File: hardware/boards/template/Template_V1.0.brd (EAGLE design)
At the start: 42 x 42 mm, 2 parts

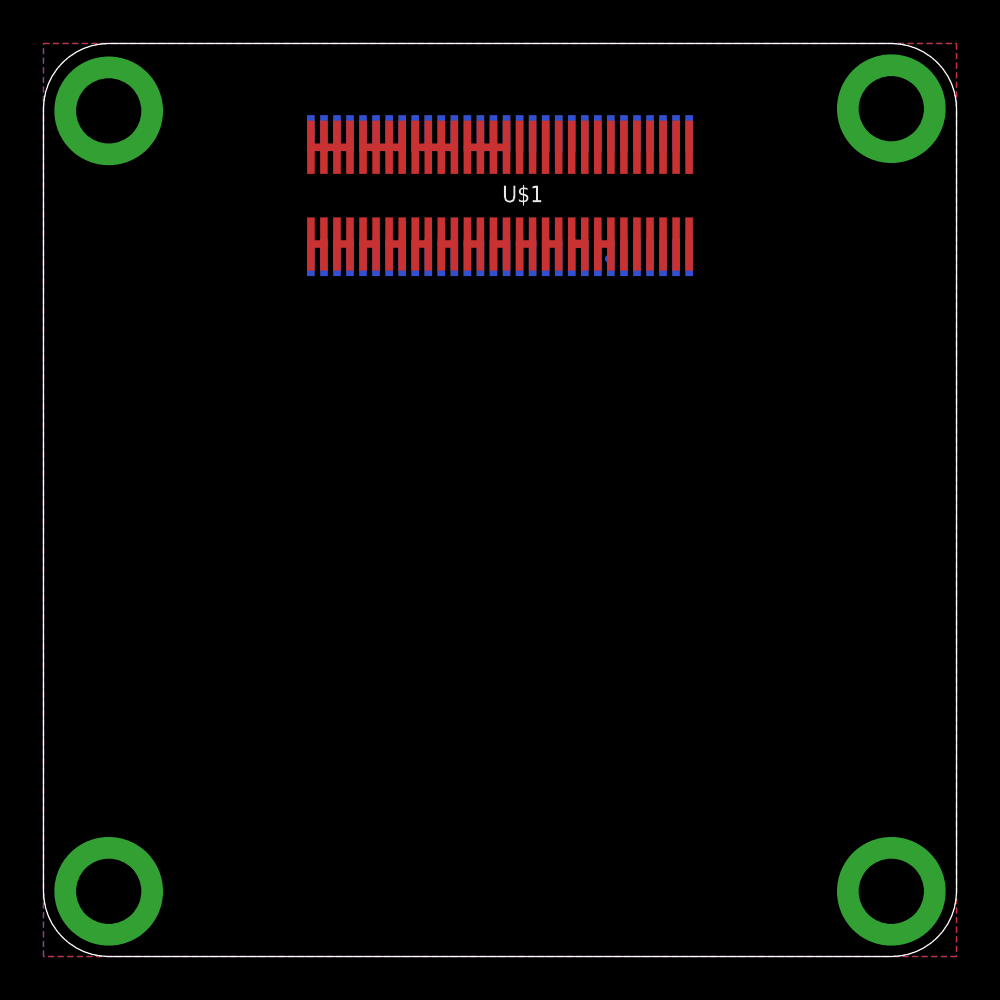
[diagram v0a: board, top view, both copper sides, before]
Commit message: Finished updating to new PQ60 V1.1 standard
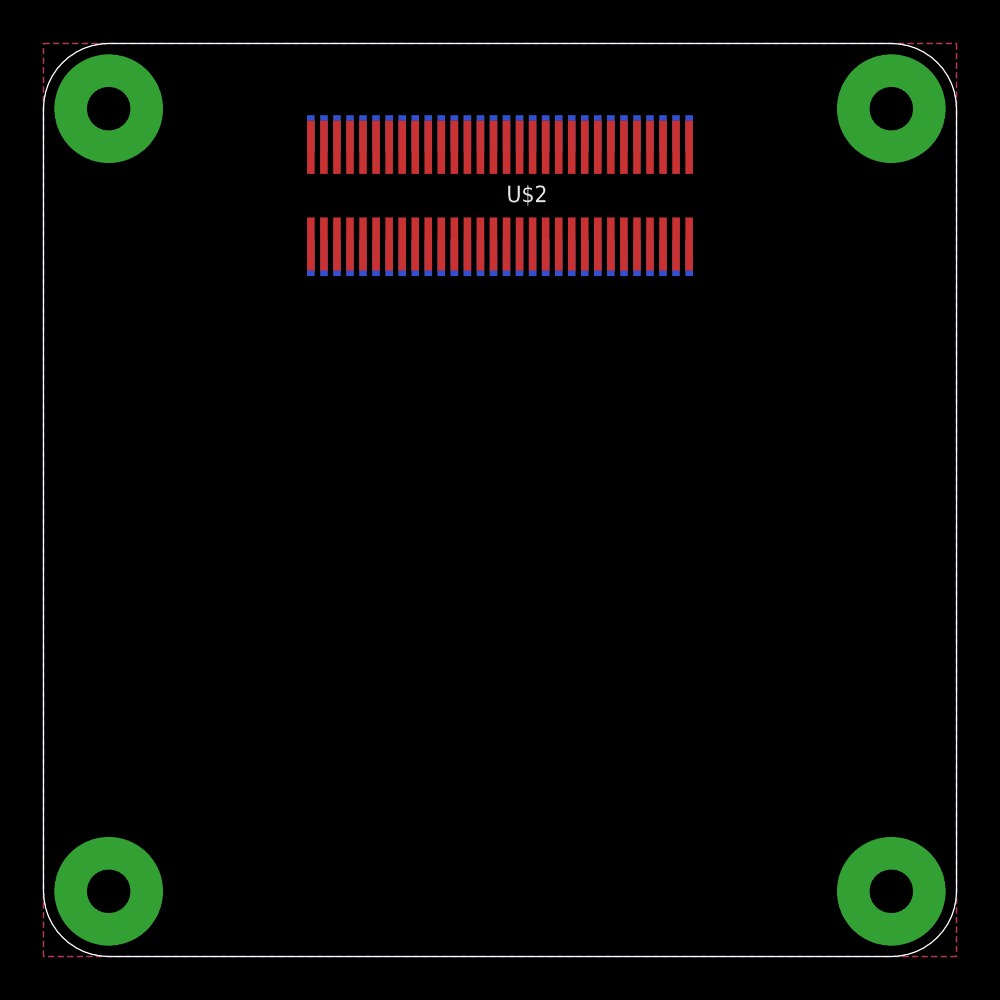
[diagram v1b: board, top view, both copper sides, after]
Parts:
- removed U$3: FX8C-060S-SV(92), PQ_components:FX8C-060S-SV(92)
- added U$2: FX8C-060P-SV(92), Template:FX8C-060P-SV(92)
- U$1: value FX8C-060P-SV(92) -> FX8C-060S-SV(92); device PQ_components:FX8C-060P-SV(92) -> Template:FX8C-060S-SV(92)
- flipped U$1 to the bottom, turned to 180 degrees
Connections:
- removed net +3.3V_1: U$3.P$22
- removed net +3.3V_2: U$3.P$21
- removed net +3.3V_3: U$3.P$20
- removed net 33-GND: U$3.P$3
- removed net 37-GND: U$3.P$7
- removed net 41-GND: U$3.P$11
- removed net 44-GND: U$3.P$14
- removed net 46-GND: U$3.P$16
- removed net 48-GND: U$3.P$18
- removed net 49-GND: U$3.P$19
- removed net 57-GND: U$3.P$27
- removed net 59-GND: U$3.P$29
- removed net VBUS2: U$3.P$24
- net +3.3V_SW1: now also U$2.P$1, U$2.P$2; no longer U$3.P$59, U$3.P$60
- net +3V3_BUS: now also U$2.P$57, U$2.P$58, U$2.P$59, U$2.P$60
- net +3V3_SW2: now also U$2.P$5, U$2.P$6; no longer U$3.P$55, U$3.P$56
- net +3V3_SW3: now also U$2.P$10, U$2.P$9; no longer U$3.P$51, U$3.P$52
- net /RST: now also U$2.P$27; no longer U$3.P$34
- net /SS/GPIO2: now also U$2.P$34
- net BATV_BUS: now also U$2.P$49, U$2.P$50, U$2.P$51, U$2.P$52
- net BATV_SW1: now also U$2.P$13, U$2.P$14; no longer U$3.P$47, U$3.P$48
- net BATV_SW2: now also U$2.P$17, U$2.P$18; no longer U$3.P$43, U$3.P$44
- net BATV_SW3: now also U$2.P$21, U$2.P$22; no longer U$3.P$39, U$3.P$40
- net GND: now also U$2.P$28; no longer U$3.P$33
- net GPIO0: now also U$2.P$25; no longer U$3.P$36
- net GPIO1: now also U$2.P$26; no longer U$3.P$35
- net GPIO10: now also U$2.P$42
- net GPIO11: now also U$2.P$43
- net GPIO12: now also U$2.P$44
- net GPIO3: now also U$2.P$35
- net GPIO4: now also U$2.P$36
- net GPIO5: now also U$2.P$37
- net GPIO6: now also U$2.P$38
- net GPIO7: now also U$2.P$39
- net GPIO8: now also U$2.P$40
- net GPIO9: now also U$2.P$41
- net MISO: now also U$2.P$32
- net MOSI: now also U$2.P$31
- net RTN_+3V3: now also U$2.P$53, U$2.P$54, U$2.P$55, U$2.P$56
- net RTN_+3V3_SW1: now also U$2.P$3, U$2.P$4; no longer U$3.P$57, U$3.P$58
- net RTN_+3V3_SW2: now also U$2.P$7, U$2.P$8; no longer U$3.P$53, U$3.P$54
- net RTN_+3V3_SW3: now also U$2.P$11, U$2.P$12; no longer U$3.P$49, U$3.P$50
- net RTN_BATV: now also U$2.P$45, U$2.P$46, U$2.P$47, U$2.P$48
- net RTN_BATV_SW1: now also U$2.P$15, U$2.P$16; no longer U$3.P$45, U$3.P$46
- net RTN_BATV_SW2: now also U$2.P$19, U$2.P$20; no longer U$3.P$41, U$3.P$42
- net RTN_BATV_SW3: now also U$2.P$23, U$2.P$24; no longer U$3.P$37, U$3.P$38
- net SCK: now also U$2.P$33
- net SCL: now also U$2.P$29; no longer U$3.P$32
- net SDA: now also U$2.P$30; no longer U$3.P$31
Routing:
- net RTN_BATV: track 1.80 -> 0.00 mm
- net RTN_+3V3: track 1.80 -> 0.00 mm
- net +3V3_BUS: track 1.80 -> 0.00 mm
- net BATV_BUS: track 1.80 -> 0.00 mm
- net BATV_SW3: track 1.11 -> 0.00 mm
- net RTN_BATV_SW3: track 0.72 -> 0.00 mm
- net RTN_BATV_SW1: track 0.60 -> 0.00 mm
- net BATV_SW2: track 0.60 -> 0.00 mm
- net BATV_SW1: track 0.60 -> 0.00 mm
- net +3V3_SW2: track 0.60 -> 0.00 mm
- net RTN_+3V3_SW2: track 0.60 -> 0.00 mm
- net RTN_+3V3_SW1: track 0.60 -> 0.00 mm
- net +3.3V_SW1: track 0.60 -> 0.00 mm
- net RTN_BATV_SW2: track 0.60 -> 0.00 mm
- net RTN_+3V3_SW3: track 0.60 -> 0.00 mm
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- added copper zone on layer 1, net BOARD
- added copper zone on layer 16, net BOARD
- removed copper zone on layer 1, net GND
- removed copper zone on layer 16, net N$1
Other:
- board text added: "SurreyEARS Pocketqube"
- board text added: "Template Board"
- board text added: "V1.0"

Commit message: fixed fx8c symbols
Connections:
- new net +3V3_SW1: U$1.P$1
- net +3.3V_SW1: no longer U$1.P$1
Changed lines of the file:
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@@
 </signal>
 <signal name="RTN_+3V3">
+<contactref element="U$2" pad="P$53"/>
+<contactref element="U$2" pad="P$54"/>
+<contactref element="U$2" pad="P$55"/>
 <contactref element="U$2" pad="P$56"/>
-<contactref element="U$2" pad="P$55"/>
-<contactref element="U$2" pad="P$54"/>
-<contactref element="U$2" pad="P$53"/>
+<contactref element="U$1" pad="P$53"/>
+<contactref element="U$1" pad="P$54"/>
+<contactref element="U$1" pad="P$55"/>
 <contactref element="U$1" pad="P$56"/>
-<contactref element="U$1" pad="P$55"/>
-<contactref element="U$1" pad="P$54"/>
-<contactref element="U$1" pad="P$53"/>
-<wire x1="15.9" y1="37.225" x2="15.3" y2="37.225" width="0" layer="19" extent="1-1"/>
-<wire x1="16.5" y1="37.225" x2="15.9" y2="37.225" width="0" layer="19" extent="1-1"/>
+<wire x1="15.3" y1="37.225" x2="15.3" y2="37.225" width="0" layer="19" extent="1-1"/>
+<wire x1="14.7" y1="37.225" x2="15.3" y2="37.225" width="0" layer="19" extent="1-1"/>
 <wire x1="14.7" y1="37.225" x2="15.3" y2="37.225" width="0" layer="19" extent="1-1"/>
 <wire x1="15.3" y1="37.85" x2="15.3" y2="37.225" width="0" layer="19" extent="1-16"/>
-<wire x1="15.9" y1="37.85" x2="15.3" y2="37.85" width="0" layer="19" extent="16-16"/>
-<wire x1="16.5" y1="37.85" x2="15.9" y2="37.85" width="0" layer="19" extent="16-16"/>
+<wire x1="15.3" y1="37.85" x2="15.3" y2="37.85" width="0" layer="19" extent="16-16"/>
+<wire x1="14.7" y1="37.85" x2="15.3" y2="37.85" width="0" layer="19" extent="16-16"/>
 <wire x1="14.7" y1="37.85" x2="15.3" y2="37.85" width="0" layer="19" extent="16-16"/>
 </signal>
 <signal name="RTN_BATV">
+<contactref element="U$2" pad="P$45"/>
+<contactref element="U$2" pad="P$46"/>
+<contactref element="U$2" pad="P$47"/>
 <contactref element="U$2" pad="P$48"/>
-<contactref element="U$2" pad="P$47"/>
-<contactref element="U$2" pad="P$46"/>
-<contactref element="U$2" pad="P$45"/>
+<contactref element="U$1" pad="P$45"/>
+<contactref element="U$1" pad="P$46"/>
+<contactref element="U$1" pad="P$47"/>
 <contactref element="U$1" pad="P$48"/>
-<contactref element="U$1" pad="P$47"/>
-<contactref element="U$1" pad="P$46"/>
-<contactref element="U$1" pad="P$45"/>
-<wire x1="21.3" y1="37.225" x2="20.7" y2="37.225" width="0" layer="19" extent="1-1"/>
-<wire x1="20.1" y1="37.225" x2="20.7" y2="37.225" width="0" layer="19" extent="1-1"/>
 <wire x1="19.5" y1="37.225" x2="20.1" y2="37.225" width="0" layer="19" extent="1-1"/>
-<wire x1="20.7" y1="37.85" x2="20.7" y2="37.225" width="0" layer="19" extent="1-16"/>
-<wire x1="21.3" y1="37.85" x2="20.7" y2="37.85" width="0" layer="19" extent="16-16"/>
-<wire x1="20.1" y1="37.85" x2="20.7" y2="37.85" width="0" layer="19" extent="16-16"/>
+<wire x1="20.1" y1="37.225" x2="20.1" y2="37.225" width="0" layer="19" extent="1-1"/>
+<wire x1="19.5" y1="37.225" x2="20.1" y2="37.225" width="0" layer="19" extent="1-1"/>
+<wire x1="20.1" y1="37.85" x2="20.1" y2="37.225" width="0" layer="19" extent="1-16"/>
+<wire x1="19.5" y1="37.85" x2="20.1" y2="37.85" width="0" layer="19" extent="16-16"/>
+<wire x1="20.1" y1="37.85" x2="20.1" y2="37.85" width="0" layer="19" extent="16-16"/>
 <wire x1="19.5" y1="37.85" x2="20.1" y2="37.85" width="0" layer="19" extent="16-16"/>
 </signal>
@@
 </signal>
 <signal name="BATV_BUS">
+<contactref element="U$2" pad="P$52"/>
+<contactref element="U$2" pad="P$51"/>
+<contactref element="U$2" pad="P$50"/>
 <contactref element="U$2" pad="P$49"/>
-<contactref element="U$2" pad="P$50"/>
-<contactref element="U$2" pad="P$51"/>
-<contactref element="U$2" pad="P$52"/>
+<contactref element="U$1" pad="P$52"/>
+<contactref element="U$1" pad="P$51"/>
+<contactref element="U$1" pad="P$50"/>
 <contactref element="U$1" pad="P$49"/>
-<contactref element="U$1" pad="P$50"/>
-<contactref element="U$1" pad="P$51"/>
-<contactref element="U$1" pad="P$52"/>
 <wire x1="18.3" y1="37.225" x2="18.9" y2="37.225" width="0" layer="19" extent="1-1"/>
-<wire x1="17.7" y1="37.225" x2="18.3" y2="37.225" width="0" layer="19" extent="1-1"/>
-<wire x1="17.1" y1="37.225" x2="17.7" y2="37.225" width="0" layer="19" extent="1-1"/>
+<wire x1="18.3" y1="37.225" x2="18.3" y2="37.225" width="0" layer="19" extent="1-1"/>
+<wire x1="18.9" y1="37.225" x2="18.3" y2="37.225" width="0" layer="19" extent="1-1"/>
 <wire x1="18.9" y1="37.85" x2="18.9" y2="37.225" width="0" layer="19" extent="1-16"/>
 <wire x1="18.3" y1="37.85" x2="18.9" y2="37.85" width="0" layer="19" extent="16-16"/>
-<wire x1="17.7" y1="37.85" x2="18.3" y2="37.85" width="0" layer="19" extent="16-16"/>
-<wire x1="17.1" y1="37.85" x2="17.7" y2="37.85" width="0" layer="19" extent="16-16"/>
+<wire x1="18.3" y1="37.85" x2="18.3" y2="37.85" width="0" layer="19" extent="16-16"/>
+<wire x1="18.9" y1="37.85" x2="18.3" y2="37.85" width="0" layer="19" extent="16-16"/>
 </signal>
 <signal name="GPIO12">
@@
 </signal>
 <signal name="+3V3_BUS">
+<contactref element="U$2" pad="P$60"/>
+<contactref element="U$2" pad="P$59"/>
+<contactref element="U$2" pad="P$58"/>
 <contactref element="U$2" pad="P$57"/>
-<contactref element="U$2" pad="P$58"/>
-<contactref element="U$2" pad="P$59"/>
-<contactref element="U$2" pad="P$60"/>
+<contactref element="U$1" pad="P$60"/>
+<contactref element="U$1" pad="P$59"/>
+<contactref element="U$1" pad="P$58"/>
 <contactref element="U$1" pad="P$57"/>
-<contactref element="U$1" pad="P$58"/>
-<contactref element="U$1" pad="P$59"/>
-<contactref element="U$1" pad="P$60"/>
 <wire x1="13.5" y1="37.225" x2="14.1" y2="37.225" width="0" layer="19" extent="1-1"/>
-<wire x1="12.9" y1="37.225" x2="13.5" y2="37.225" width="0" layer="19" extent="1-1"/>
-<wire x1="12.3" y1="37.225" x2="12.9" y2="37.225" width="0" layer="19" extent="1-1"/>
+<wire x1="13.5" y1="37.225" x2="13.5" y2="37.225" width="0" layer="19" extent="1-1"/>
+<wire x1="14.1" y1="37.225" x2="13.5" y2="37.225" width="0" layer="19" extent="1-1"/>
 <wire x1="14.1" y1="37.85" x2="14.1" y2="37.225" width="0" layer="19" extent="1-16"/>
 <wire x1="13.5" y1="37.85" x2="14.1" y2="37.85" width="0" layer="19" extent="16-16"/>
-<wire x1="12.9" y1="37.85" x2="13.5" y2="37.85" width="0" layer="19" extent="16-16"/>
-<wire x1="12.3" y1="37.85" x2="12.9" y2="37.85" width="0" layer="19" extent="16-16"/>
+<wire x1="13.5" y1="37.85" x2="13.5" y2="37.85" width="0" layer="19" extent="16-16"/>
+<wire x1="14.1" y1="37.85" x2="13.5" y2="37.85" width="0" layer="19" extent="16-16"/>
 </signal>
 <signal name="GPIO8">
@@
 <contactref element="U$2" pad="P$1"/>
 <contactref element="U$2" pad="P$2"/>
-<contactref element="U$1" pad="P$1"/>
 <contactref element="U$1" pad="P$2"/>
 <wire x1="12.3" y1="32.775" x2="12.9" y2="32.775" width="0" layer="19" extent="1-1"/>
 <wire x1="12.9" y1="32.15" x2="12.9" y2="32.775" width="0" layer="19" extent="1-16"/>
-<wire x1="12.3" y1="32.15" x2="12.9" y2="32.15" width="0" layer="19" extent="16-16"/>
 </signal>
 <signal name="GPIO1">
@@
 <wire x1="28.5" y1="32.15" x2="28.5" y2="32.775" width="0" layer="19" extent="1-16"/>
 </signal>
+<signal name="+3V3_SW1">
+<contactref element="U$1" pad="P$1"/>
+</signal>
 </signals>
